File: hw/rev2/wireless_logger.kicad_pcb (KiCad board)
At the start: 4 copper layers, 30 x 50 mm, 147 parts, among them J1 FCI 10118194, J2 CONN_2, J3 SSD1306_SER, J4 SWD_10PIN, J5 CONN_5, J6 CONN_6X2, Q1 2N7002P, Q2 2N7002P, U1 MT29FXX01A, U10 CC2541, U11 STM32F40X_BGA176, U2 MAG3110, U3 MMA8452Q, U4 LPS331AP, U5 L3GD20, U6 MCP111T-315, U7 BQ24095, U8 TPS62698, U9 CC1101, X1 FA-128 26.0000MF10Z-W3, X2 9HT10-32.768KBZF-T, X3 FA-128 32.0000MF20X-K3, X4 XRCGB25M000F0L00R0, X5 9HT10-32.768KBZF-T

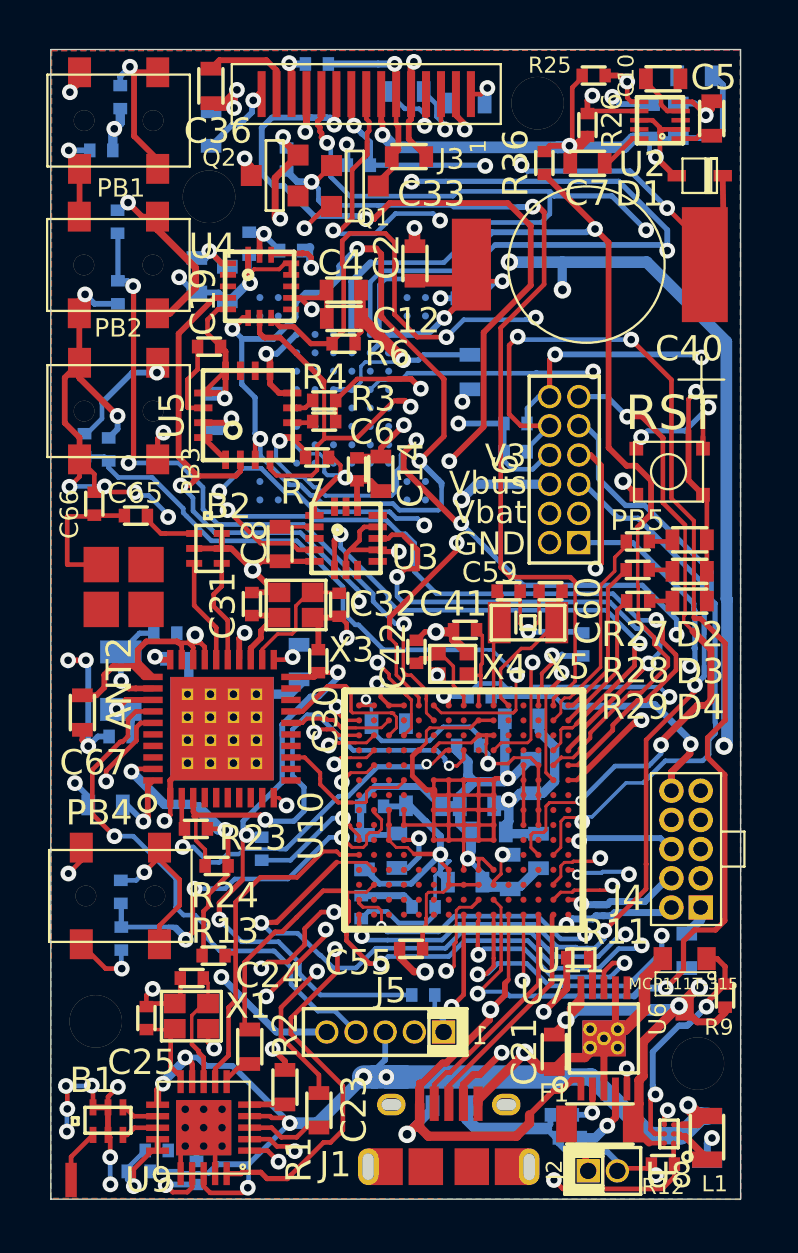
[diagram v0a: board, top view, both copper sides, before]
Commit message: Added isolation for flash power and battery voltage monitoring
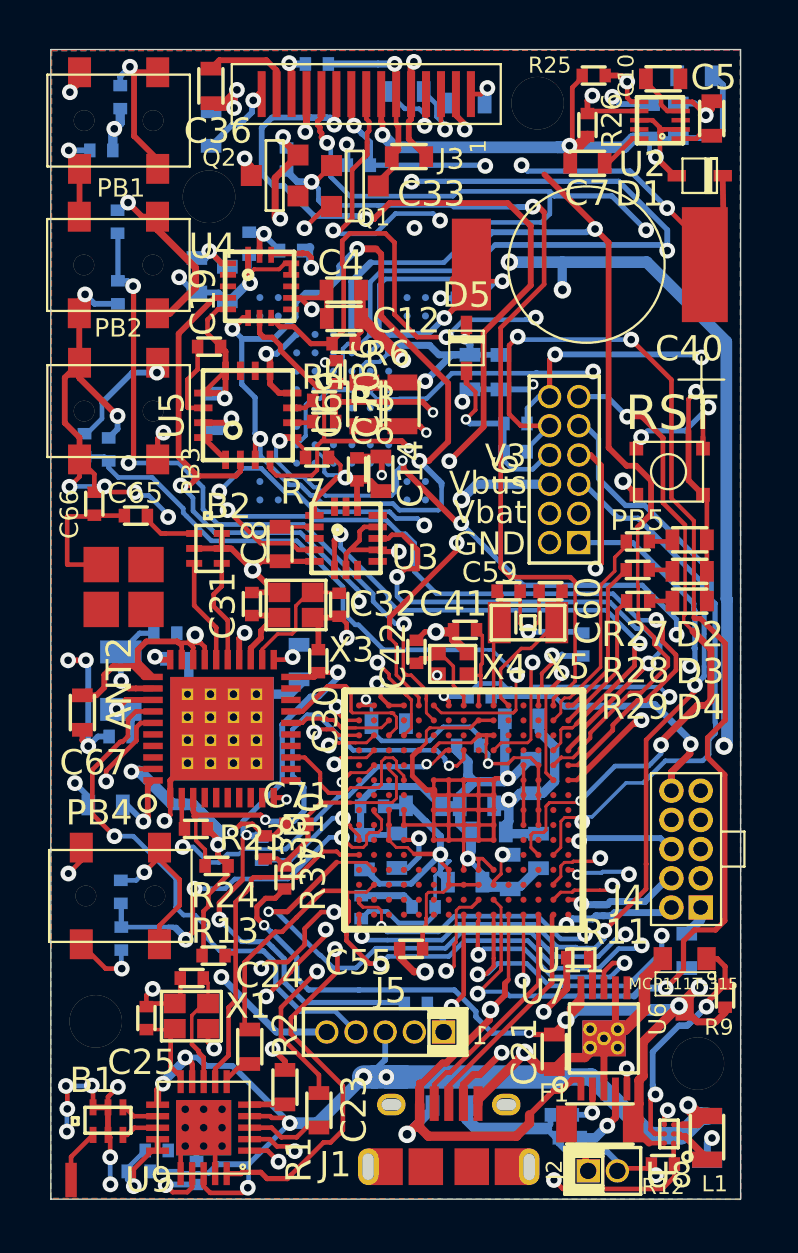
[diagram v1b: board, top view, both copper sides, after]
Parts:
- added C69: 10u, SMD0805, F.Cu at (183.6, 125.4)
- added C70: 10u, SMD0805, F.Cu at (185.3, 125.4)
- added C71: 1u, SMD0402, F.Cu at (180.7, 143.7)
- added D5: BAT43XV2, SOD-523F, F.Cu at (188.1, 123.0)
- added R37: 1M, SMD0402, F.Cu at (180.2, 146.0)
- added R38: 1M, SMD0402, F.Cu at (179.3, 144.7)
- C1: value CAP -> 0.1u
- C2: value CAP -> 1u; moved to B.Cu
- moved R36 12.8 mm to (182.4, 124.0), turned to 270 degrees
- moved C2 6.03 mm to (189.6, 124.0)
- moved R16 0.49 mm to (185.9, 151.5)
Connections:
- C1 pad 2: V3 -> /V3_FLASH
- C2 pad 2: V3 -> /V3_FLASH
- R36 pad 2: V3 -> /V3_FLASH
- U1 pad D3: V3 -> /V3_FLASH
- U1 pad G5: V3 -> /V3_FLASH
- U1 pad G6: V3 -> /V3_FLASH
- U1 pad J8: V3 -> /V3_FLASH
- U11 pad N5: (no net) -> N-0000092
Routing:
- net /V3_FLASH: track 0.00 -> 19.2 mm, vias 0 -> 2
- net Vbat: track 91.6 -> 109.4 mm, vias 7 -> 9
- net N-0000092: track 0.00 -> 9.31 mm
- net GND: track 282.3 -> 288.0 mm, vias 56 -> 59
- net /Sensors/GYR_SPI_MISO: track 62.1 -> 56.5 mm
- net /STM32F4/FLASH_nCS: track 44.5 -> 47.7 mm, vias 1 -> 2
- net V3: track 332.1 -> 329.5 mm
- net /STM32F4/GYRO_nCS: track 40.0 -> 37.8 mm
- net /STM32F4/EXTI2: track 6.71 -> 7.76 mm
- net /STM32F4/EXTI1: track 24.7 -> 23.7 mm
- net /STM32F4/SPI2_NSS: track 53.5 -> 52.9 mm
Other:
- board text added: "Strike Force rev 2b"
- board text removed: "Strike Force rev 2a"

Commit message: Finished more small connections
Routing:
- net GND: track 288.0 -> 288.7 mm
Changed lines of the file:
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@@
   (general
     (links 490)
-    (no_connects 1)
-    (area 169.994999 109.994999 200.005001 160.005001)
+    (no_connects 0)
+    (area 162.356596 104.978178 209.633231 164.898333)
     (thickness 1.6)
     (drawings 18)
-    (tracks 3234)
+    (tracks 3236)
     (zones 0)
     (modules 153)
@@
   (layers
     (15 F.Cu signal)
-    (2 Inner2.Cu mixed)
-    (1 GND_PLANE mixed)
+    (2 Inner2.Cu mixed hide)
+    (1 GND_PLANE mixed hide)
     (0 B.Cu signal)
     (16 B.Adhes user hide)
@@
   )
   (setup
-    (last_trace_width 0.1778)
+    (last_trace_width 0.1524)
     (user_trace_width 0.127)
     (user_trace_width 0.1524)
@@
     (pad_to_mask_clearance 0)
     (aux_axis_origin 0 0)
-    (visible_elements FFFF7F8F)
+    (visible_elements FFFF7FAF)
     (pcbplotparams
       (layerselection 284196871)
@@
   (segment (start 189.63641 131.419884) (end 189.63641 122.14859) (width 0.2032) (layer Inner2.Cu) (net 60))
   (segment (start 189.63641 122.14859) (end 190.08852 121.69648) (width 0.2032) (layer Inner2.Cu) (net 60))
-  (segment (start 188.07684 121.97842) (end 188.07684 122.51055) (width 0.3048) (layer F.Cu) (net 61) (status 400000))
-  (segment (start 188.22924 122.83059) (end 188.22924 123.2782) (width 0.3048) (layer B.Cu) (net 61) (status 800000))
+  (segment (start 188.07684 121.97842) (end 188.07684 122.51055) (width 0.3048) (layer F.Cu) (net 61))
+  (segment (start 188.22924 122.83059) (end 188.22924 123.2782) (width 0.3048) (layer B.Cu) (net 61))
   (segment (start 187.99302 122.59437) (end 188.22924 122.83059) (width 0.3048) (layer B.Cu) (net 61))
   (via (at 187.99302 122.59437) (size 0.4572) (drill 0.254) (layers F.Cu B.Cu) (net 61))
@@
   (segment (start 185.28919 124.48536) (end 185.29173 124.48282) (width 0.254) (layer F.Cu) (net 61))
   (segment (start 182.29326 124.7902) (end 183.09336 124.7902) (width 0.2286) (layer B.Cu) (net 61) (status 40030))
+  (segment (start 189.88024 141.69644) (end 190.47652 141.69644) (width 0.1524) (layer F.Cu) (net 62) (status 800000))
+  (segment (start 190.47652 141.69644) (end 190.5566 141.77652) (width 0.1524) (layer F.Cu) (net 62) (status C00000))
   (segment (start 189.57544 124.78328) (end 190.76092 124.78328) (width 0.254) (layer B.Cu) (net 62))
   (via (at 190.9826 124.5616) (size 0.4572) (drill 0.254) (layers F.Cu B.Cu) (net 62))
@@
   (segment (start 185.03138 141.63421) (end 185.03138 142.56639) (width 0.127) (layer F.Cu) (net 112))
   (segment (start 184.7066 141.30943) (end 185.03138 141.63421) (width 0.127) (layer F.Cu) (net 112))
-  (segment (start 188.07684 123.9774) (end 188.07684 124.50699) (width 0.254) (layer F.Cu) (net 113) (status 400000))
+  (segment (start 188.07684 123.9774) (end 188.07684 124.50699) (width 0.254) (layer F.Cu) (net 113))
   (segment (start 188.46927 125.67285) (end 188.05398 126.08814) (width 0.1778) (layer F.Cu) (net 113))
   (segment (start 188.46927 124.89942) (end 188.46927 125.67285) (width 0.1778) (layer F.Cu) (net 113))

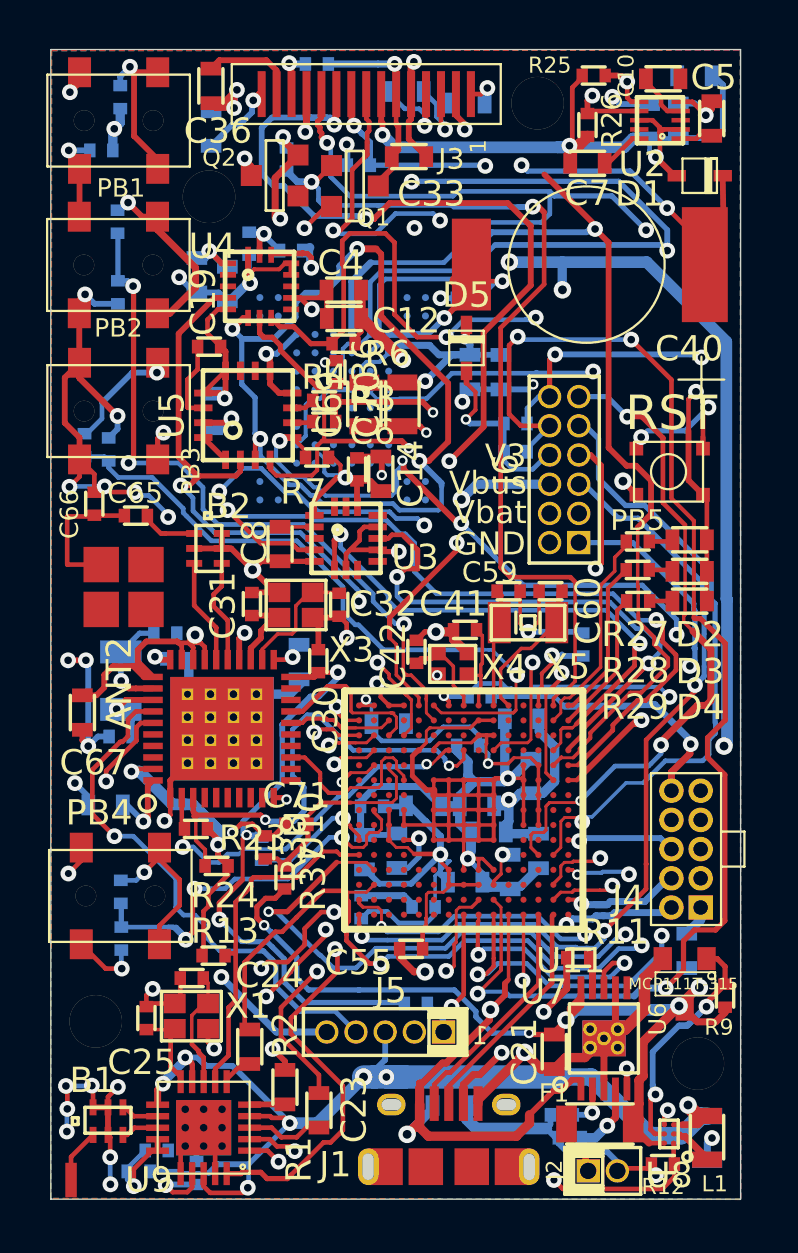
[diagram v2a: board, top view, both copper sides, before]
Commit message: Added super-slick graphics and standardized silk print sizes
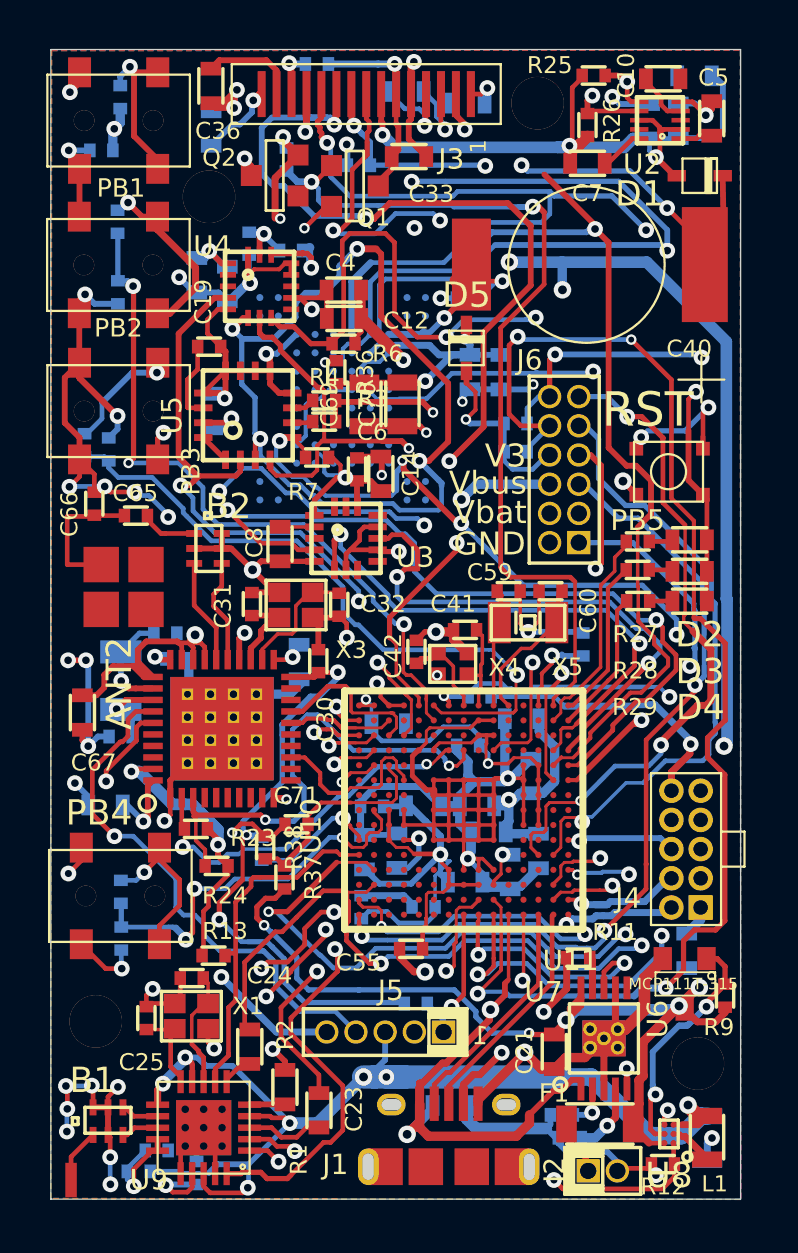
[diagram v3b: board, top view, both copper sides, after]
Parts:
- added VAL: MCGILL, MCGILL, B.Cu at (195.8, 122.1)
- added VAL: EAGLE, EAGLE, B.Cu at (190.3, 116.6)
- added VAL: OSHW, OSHW, B.Cu at (177.0, 150.7)
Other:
- board text added: "FORCE"
- board text added: "STRIKE"
- board text added: "rev 2b"
- board text removed: "Strike Force rev 2b"

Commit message: Moved to NSMD BGA mounting and moved silks around.
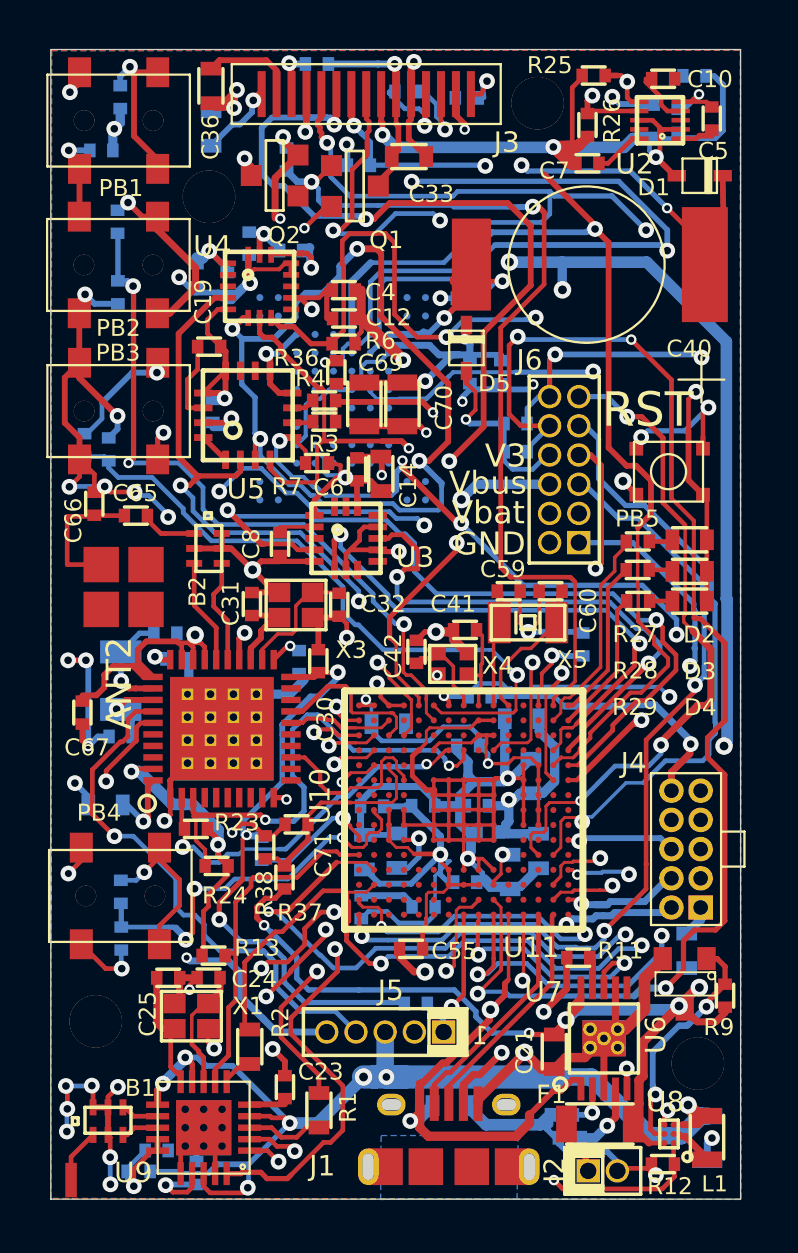
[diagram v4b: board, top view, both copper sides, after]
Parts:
- C1, C10, C11, C12, C15, C17, C18, C2, C23, C34, C35, C4, C5, C50, C51, C52, C53, C67, C68, C7, C8, C9: footprint SMD0603 -> SMD0402
- moved C25 1.99 mm to (175.1, 150.4), turned to 180 degrees
- moved C24 0.73 mm to (176.9, 150.4)
- moved R7 0.24 mm to (181.6, 128.0)
- moved C34 0.23 mm to (188.1, 112.1)
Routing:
- net V3: track 329.5 -> 331.8 mm, vias 28 -> 27
- net /Bluetooth/RF_DD: track 20.1 -> 21.8 mm
- net N-00000195: track 3.80 -> 5.40 mm
- net Vbus: track 52.8 -> 51.7 mm
- added copper zone on B.Cu, net (none)
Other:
- board text added: "BRN"
- board text added: "r2b"
- board text removed: "rev 2b"
